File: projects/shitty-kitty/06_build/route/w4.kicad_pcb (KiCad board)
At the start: 4 copper layers, 130 x 75 mm, 82 parts, among them J1 DC-005C-20A 12V, J2 TYPE-C-31-M-12, J3 ELECTRODES INNER, J4 ELECTRODES OUTER, J5 MOTOR NEMA17, J6 ENDSTOP TERM, J8 HOST 1x6, Q1 AOD4185 revpol, SW1 TS-1187A BOOT, SW2 TS-1187A RESET, U1 ESP32-S3-WROOM-1-N8R2, U2 TMC2209-LA-T, U3 MPR121QR2 0x5A, U4 MPR121QR2 0x5B, U5 MPR121QR2 0x5C, U6 MPR121QR2 0x5D, U7 LIS2DH12TR, U8 AP63205WU-7, U9 AMS1117-3.3

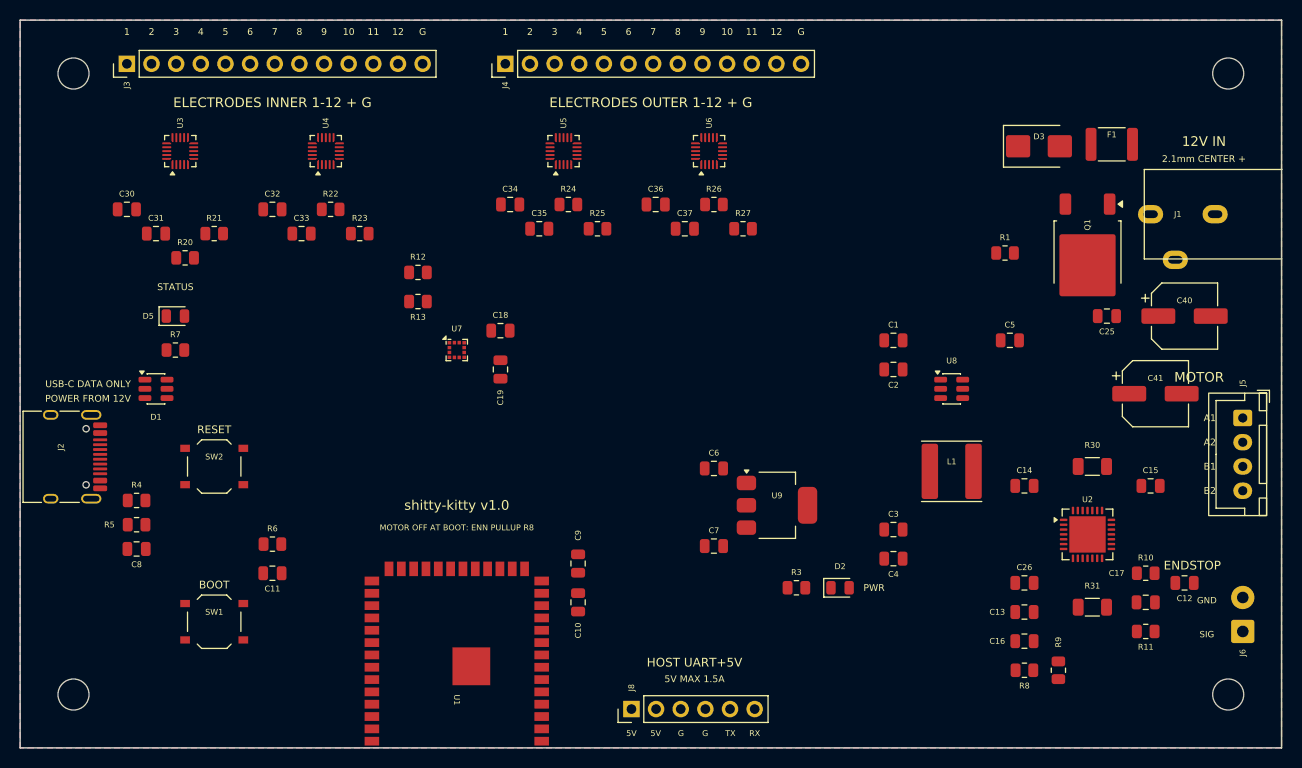
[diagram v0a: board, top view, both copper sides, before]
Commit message: shitty-kitty: route iteration — MPR121s rotated 90 (electrodes north/east, support south), single mega signal wave (intra-wave ripup arbitration), BRA/BRB ride the motor wave
Co-Authored-By: Claude Fable 5 <noreply@anthropic.com>
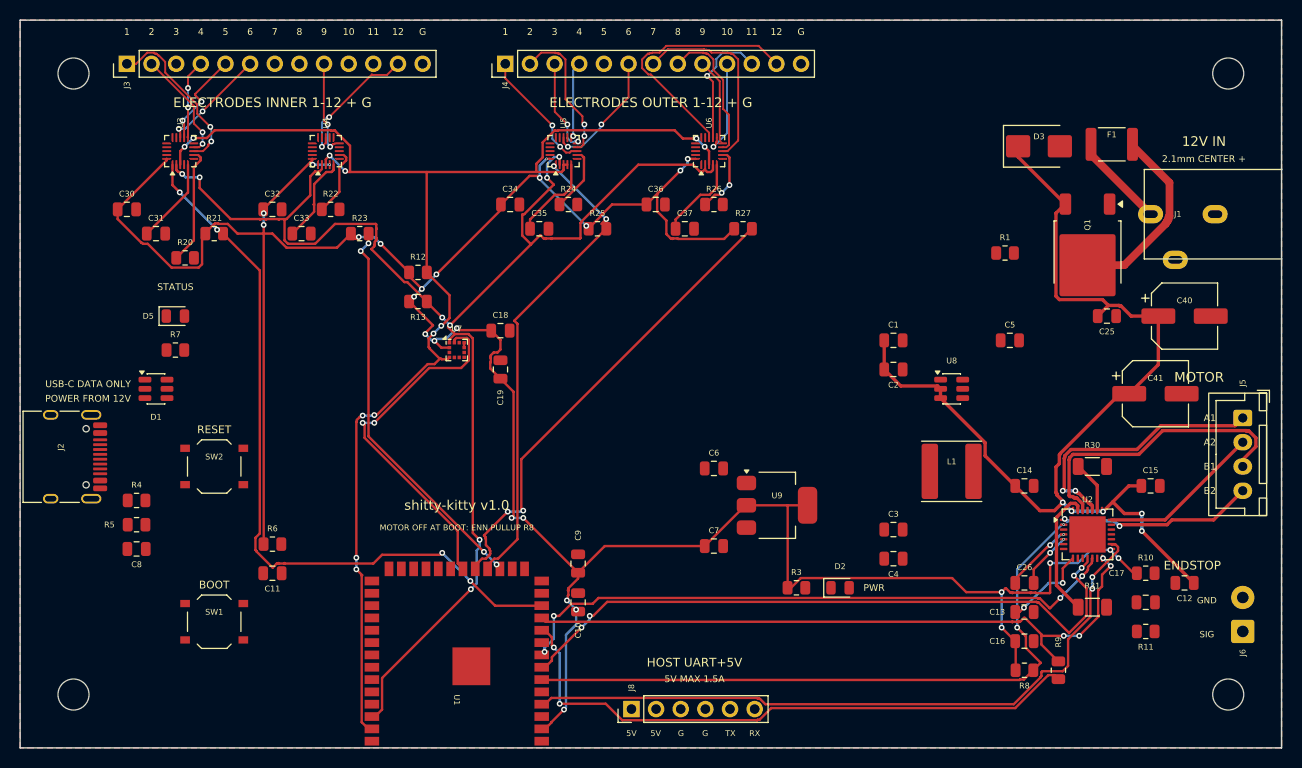
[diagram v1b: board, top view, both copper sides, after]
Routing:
- net 3V3: track 0.00 -> 300.0 mm, vias 0 -> 27
- net SCL: track 0.00 -> 146.2 mm, vias 0 -> 8
- net SDA: track 0.00 -> 139.8 mm, vias 0 -> 12
- net VIN_12V: track 0.00 -> 107.2 mm, vias 0 -> 5
- net MPR_IRQ1: track 0.00 -> 77.0 mm, vias 0 -> 4
- net STEP: track 0.00 -> 71.8 mm, vias 0 -> 2
- net TMC_UART: track 0.00 -> 69.8 mm, vias 0 -> 4
- net ENN: track 0.00 -> 69.5 mm, vias 0 -> 2
- net DIAG: track 0.00 -> 68.0 mm, vias 0 -> 4
- net INDEX: track 0.00 -> 63.8 mm, vias 0 -> 4
- net TMC_TX: track 0.00 -> 62.7 mm, vias 0 -> 2
- net MPR_IRQ3: track 0.00 -> 49.2 mm, vias 0 -> 2
- net MPR_IRQ4: track 0.00 -> 48.7 mm, vias 0 -> 2
- net MPR_IRQ2: track 0.00 -> 40.9 mm, vias 0 -> 4
- net ACC_INT: track 0.00 -> 37.0 mm, vias 0 -> 2
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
